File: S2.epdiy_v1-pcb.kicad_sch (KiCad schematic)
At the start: 93 parts, among them J2 Jack-DC, P1 CONN_02X13, Q1 MMBT3904, Q2 MMBT3904, SW1 RESET, SW2 BOOT, U1 MCP1700-3302E_SOT23, U3 QFN50P700X700X100-49N, U7 TPS2113APWR

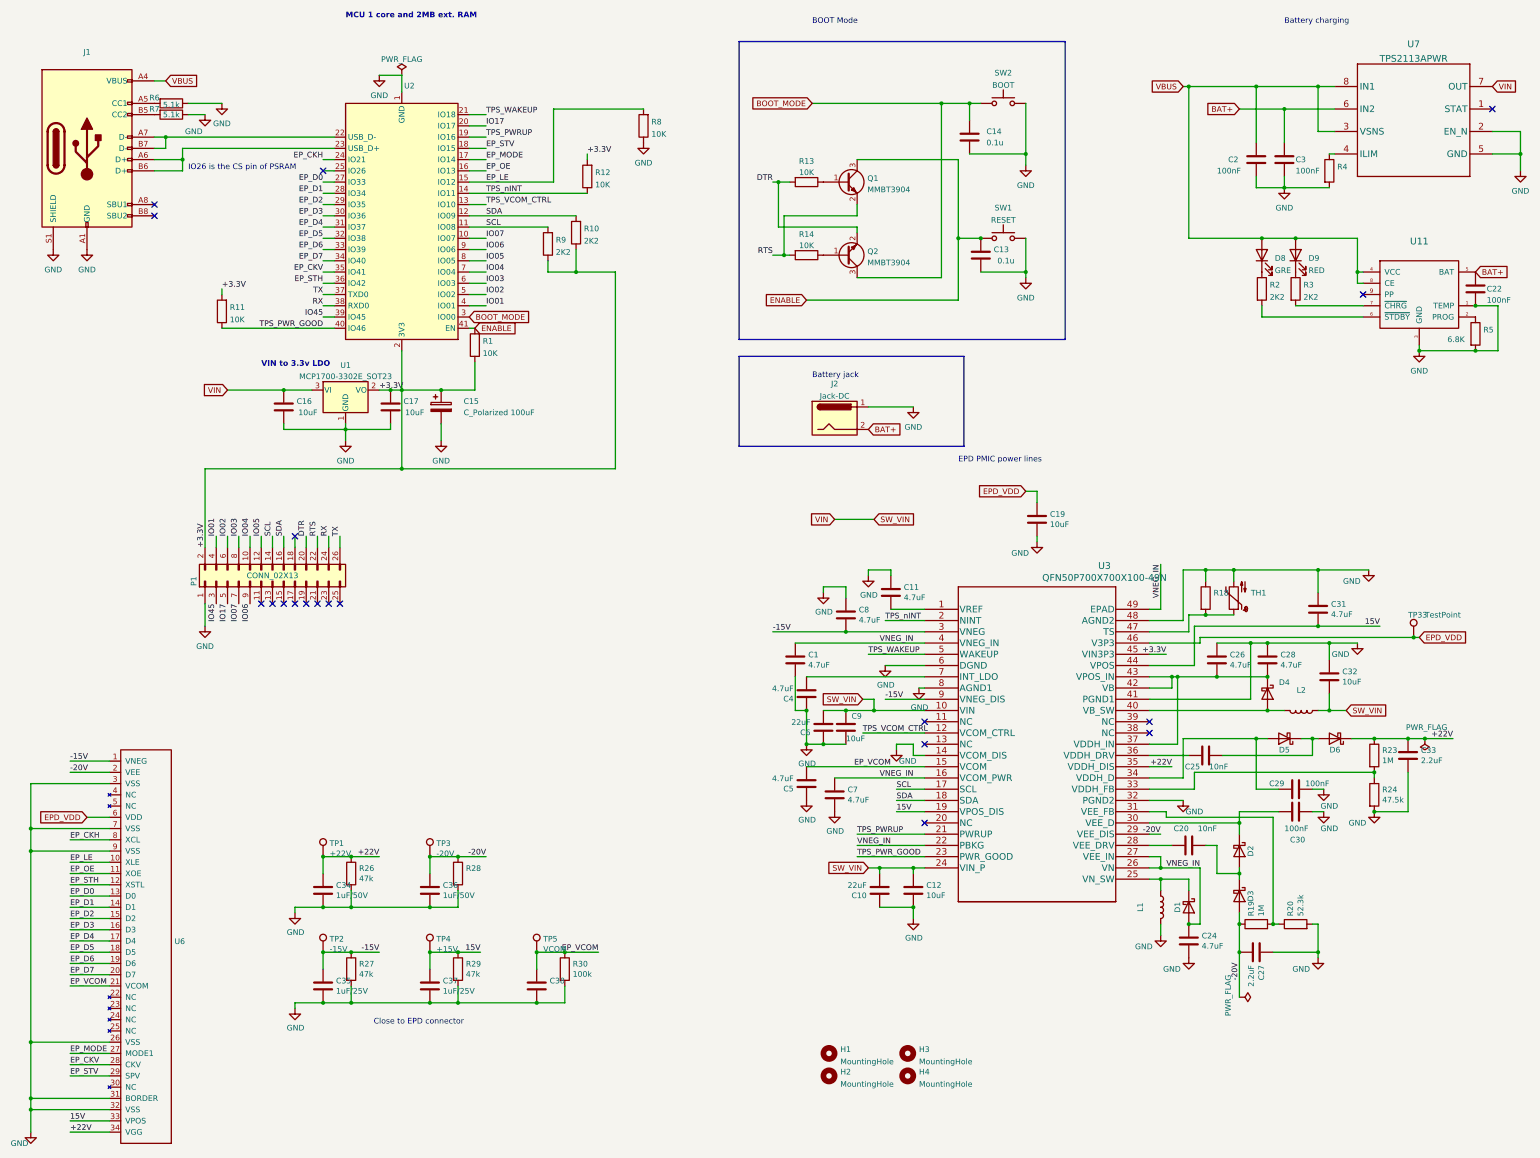
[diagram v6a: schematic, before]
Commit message: 6 10K RES wrong component 5.1Ω
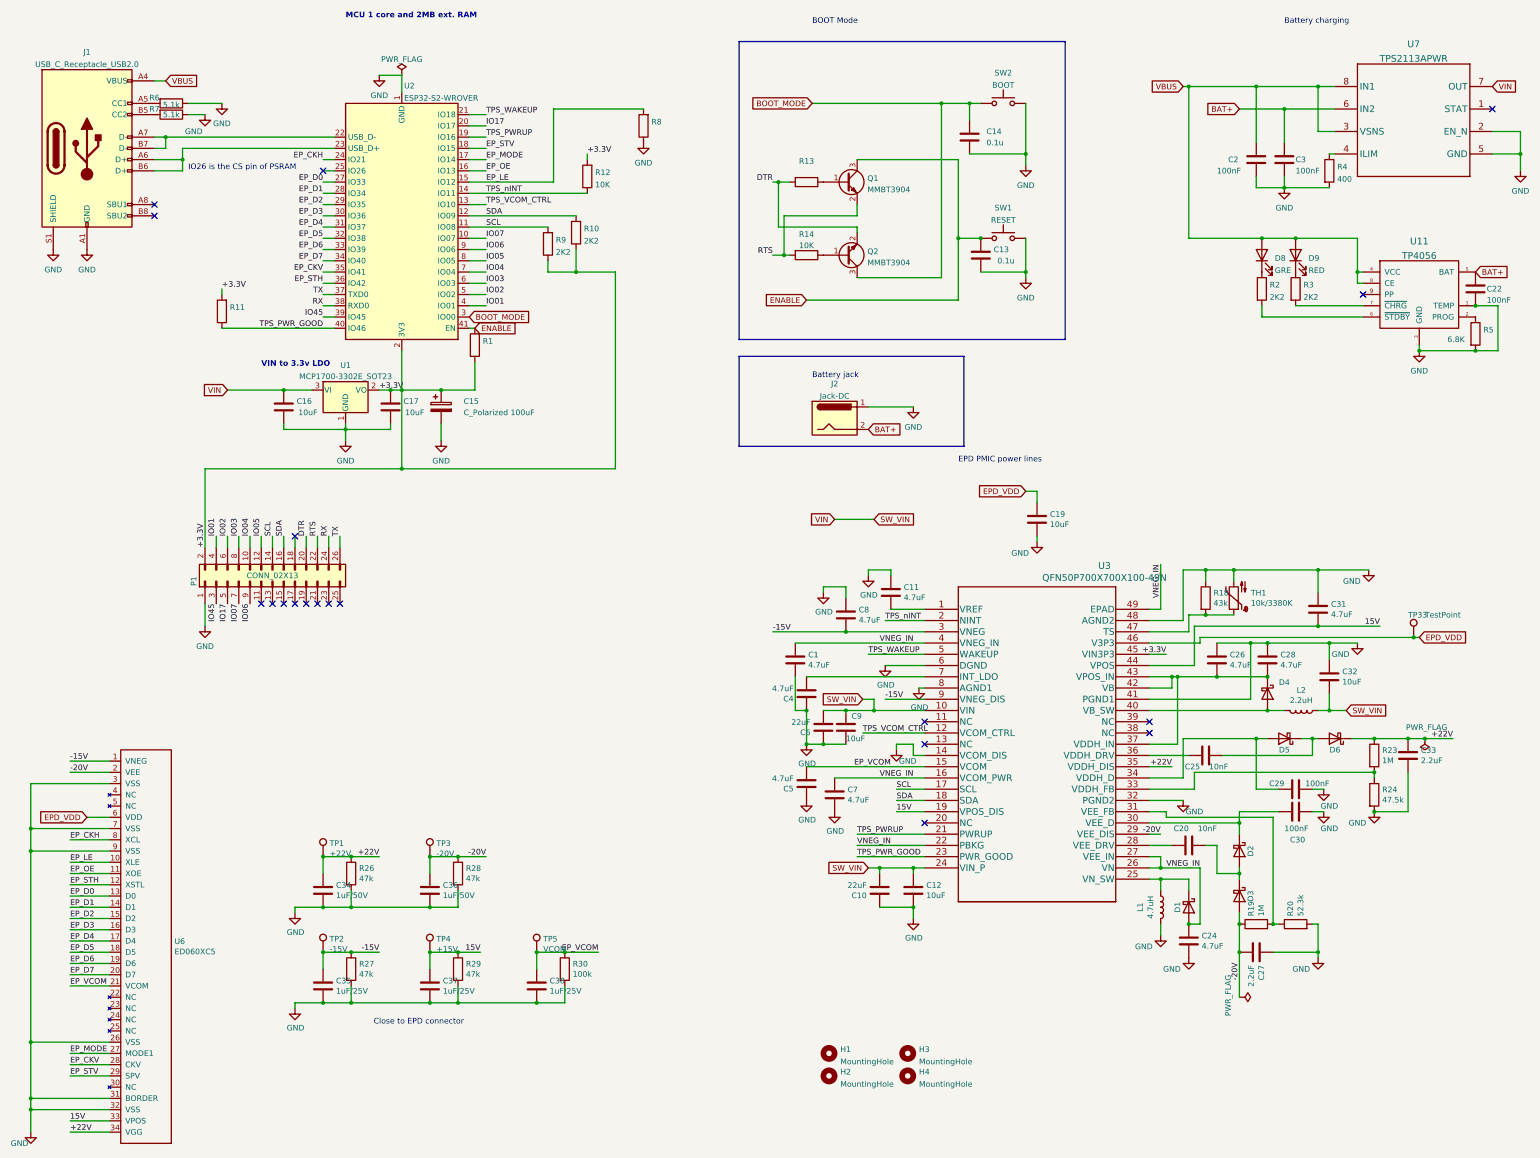
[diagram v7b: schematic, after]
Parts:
- C38: value (none) -> 1uF/25V; footprint (none) -> Capacitor_SMD:C_0805_2012Metric
- J1: value (none) -> USB_C_Receptacle_USB2.0; footprint (none) -> footprint:USB_C_Receptacle_HRO_TYPE-C-31-M-12
- L1: value (none) -> 4.7uH; footprint (none) -> Inductor_SMD:L_Taiyo-Yuden_NR-50xx_HandSoldering
- L2: value (none) -> 2.2uH; footprint (none) -> Inductor_SMD:L_Taiyo-Yuden_NR-40xx_HandSoldering
- R1, R11, R13, R8: value 10K -> (none); footprint Resistor_SMD:R_0603_1608Metric -> (none); LCSC C25197 -> C25804
- R18: value (none) -> 43k; footprint (none) -> Resistor_SMD:R_0603_1608Metric
- R28: value (none) -> 47k; footprint (none) -> Resistor_SMD:R_0603_1608Metric
- R4: value (none) -> 400; footprint (none) -> Resistor_SMD:R_0603_1608Metric
- TH1: value (none) -> 10k/3380K; footprint (none) -> Resistor_SMD:R_0603_1608Metric
- U11: value (none) -> TP4056; footprint (none) -> TP4056:TP4056_SOP-8-PP
- U2: value (none) -> ESP32-S2-WROVER; footprint (none) -> RF_Module:ESP32-S2-WROVER
- U6: value (none) -> ED060XC5; footprint (none) -> footprint:X05A20H34G
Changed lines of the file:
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@@
     (in_bom yes) (on_board yes)
     (property "Reference" "L2" (id 0) (at 335.28 173.2026 90))
-    (property "Value" "" (id 1) (at 335.28 175.514 90))
-    (property "Footprint" "" (id 2) (at 335.28 177.8 0)
+    (property "Value" "2.2uH" (id 1) (at 335.28 175.514 90))
+    (property "Footprint" "Inductor_SMD:L_Taiyo-Yuden_NR-40xx_HandSoldering" (id 2) (at 335.28 177.8 0)
       (effects (font (size 1.27 1.27)) hide)
     )
@@
       (effects (font (size 1.27 1.27)) (justify left))
     )
-    (property "Value" "" (id 1) (at 80.7212 232.283 0)
-      (effects (font (size 1.27 1.27)) (justify left))
-    )
-    (property "Footprint" "" (id 2) (at 67.31 184.15 0)
+    (property "Value" "ED060XC5" (id 1) (at 80.7212 232.283 0)
+      (effects (font (size 1.27 1.27)) (justify left))
+    )
+    (property "Footprint" "footprint:X05A20H34G" (id 2) (at 67.31 184.15 0)
       (effects (font (size 1.27 1.27)) hide)
     )
@@
       (effects (font (size 1.27 1.27)) (justify right))
     )
-    (property "Value" "" (id 1) (at 323.9008 153.543 0)
-      (effects (font (size 1.27 1.27)) (justify right))
-    )
-    (property "Footprint" "" (id 2) (at 320.04 153.67 0)
+    (property "Value" "10k/3380K" (id 1) (at 323.9008 153.543 0)
+      (effects (font (size 1.27 1.27)) (justify right))
+    )
+    (property "Footprint" "Resistor_SMD:R_0603_1608Metric" (id 2) (at 320.04 153.67 0)
       (effects (font (size 1.27 1.27)) hide)
     )
@@
       (effects (font (size 1.27 1.27)) (justify left))
     )
-    (property "Value" "" (id 1) (at 315.468 153.543 0)
-      (effects (font (size 1.27 1.27)) (justify left))
-    )
-    (property "Footprint" "" (id 2) (at 311.912 152.4 90)
+    (property "Value" "43k" (id 1) (at 315.468 153.543 0)
+      (effects (font (size 1.27 1.27)) (justify left))
+    )
+    (property "Footprint" "Resistor_SMD:R_0603_1608Metric" (id 2) (at 311.912 152.4 90)
       (effects (font (size 1.27 1.27)) hide)
     )
@@
     (in_bom yes) (on_board yes)
     (property "Reference" "L1" (id 0) (at 298.9326 222.25 90))
-    (property "Value" "" (id 1) (at 301.244 222.25 90))
-    (property "Footprint" "" (id 2) (at 303.53 222.25 0)
+    (property "Value" "4.7uH" (id 1) (at 301.244 222.25 90))
+    (property "Footprint" "Inductor_SMD:L_Taiyo-Yuden_NR-50xx_HandSoldering" (id 2) (at 303.53 222.25 0)
       (effects (font (size 1.27 1.27)) hide)
     )
@@
       (effects (font (size 1.27 1.27)) (justify left))
     )
-    (property "Value" "" (id 1) (at 146.558 215.773 0)
-      (effects (font (size 1.27 1.27)) (justify left))
-    )
-    (property "Footprint" "" (id 2) (at 143.002 214.63 90)
+    (property "Value" "47k" (id 1) (at 146.558 215.773 0)
+      (effects (font (size 1.27 1.27)) (justify left))
+    )
+    (property "Footprint" "Resistor_SMD:R_0603_1608Metric" (id 2) (at 143.002 214.63 90)
       (effects (font (size 1.27 1.27)) hide)
     )
@@
       (effects (font (size 1.27 1.27)) (justify left))
     )
-    (property "Value" "" (id 1) (at 165.481 241.173 0)
-      (effects (font (size 1.27 1.27)) (justify left))
-    )
-    (property "Footprint" "" (id 2) (at 163.5252 243.84 0)
+    (property "Value" "1uF/25V" (id 1) (at 165.481 241.173 0)
+      (effects (font (size 1.27 1.27)) (justify left))
+    )
+    (property "Footprint" "Capacitor_SMD:C_0805_2012Metric" (id 2) (at 163.5252 243.84 0)
       (effects (font (size 1.27 1.27)) hide)
     )
@@
     (in_bom yes) (on_board yes) (fields_autoplaced)
     (property "Reference" "R13" (id 0) (at 223.52 53.7042 90))
-    (property "Value" "10K" (id 1) (at 223.52 56.2411 90))
-    (property "Footprint" "Resistor_SMD:R_0603_1608Metric" (id 2) (at 223.52 56.642 90)
+    (property "Value" "" (id 1) (at 223.52 56.2411 90))
+    (property "Footprint" "" (id 2) (at 223.52 56.642 90)
       (effects (font (size 1.27 1.27)) hide)
     )
@@
       (effects (font (size 1.27 1.27)) hide)
     )
-    (property "LCSC" "C25197" (id 4) (at 223.52 58.42 90)
+    (property "LCSC" "C25804" (id 4) (at 223.52 58.42 90)
       (effects (font (size 1.27 1.27)) hide)
     )
@@
       (effects (font (size 1.27 1.27)) (justify left))
     )
-    (property "Value" "" (id 1) (at 343.408 57.7466 0)
-      (effects (font (size 1.27 1.27)) (justify left))
-    )
-    (property "Footprint" "" (id 2) (at 339.852 55.88 90)
+    (property "Value" "400" (id 1) (at 343.408 57.7466 0)
+      (effects (font (size 1.27 1.27)) (justify left))
+    )
+    (property "Footprint" "Resistor_SMD:R_0603_1608Metric" (id 2) (at 339.852 55.88 90)
       (effects (font (size 1.27 1.27)) hide)
     )
@@
       (effects (font (size 1.27 1.27)) (justify right))
     )
-    (property "Value" "" (id 1) (at 132.6006 39.4486 0)
-      (effects (font (size 1.27 1.27)) (justify right))
-    )
-    (property "Footprint" "" (id 2) (at 113.03 36.83 0)
+    (property "Value" "ESP32-S2-WROVER" (id 1) (at 132.6006 39.4486 0)
+      (effects (font (size 1.27 1.27)) (justify right))
+    )
+    (property "Footprint" "RF_Module:ESP32-S2-WROVER" (id 2) (at 113.03 36.83 0)
       (effects (font (size 1.27 1.27)) hide)
     )
@@
       (effects (font (size 1.27 1.27)) (justify right))
     )
-    (property "Value" "10K" (id 1) (at 93.218 89.4966 0)
-      (effects (font (size 1.27 1.27)) (justify right))
-    )
-    (property "Footprint" "Resistor_SMD:R_0603_1608Metric" (id 2) (at 93.218 87.63 90)
+    (property "Value" "" (id 1) (at 93.218 89.4966 0)
+      (effects (font (size 1.27 1.27)) (justify right))
+    )
+    (property "Footprint" "" (id 2) (at 93.218 87.63 90)
       (effects (font (size 1.27 1.27)) hide)
     )
@@
       (effects (font (size 1.27 1.27)) hide)
     )
-    (property "LCSC" "C25197" (id 4) (at 91.44 87.63 0)
+    (property "LCSC" "C25804" (id 4) (at 91.44 87.63 0)
       (effects (font (size 1.27 1.27)) hide)
     )
@@
       (effects (font (size 1.27 1.27)) (justify right))
     )
-    (property "Value" "10K" (id 1) (at 188.468 47.5866 0)
-      (effects (font (size 1.27 1.27)) (justify right))
-    )
-    (property "Footprint" "Resistor_SMD:R_0603_1608Metric" (id 2) (at 188.468 45.72 90)
+    (property "Value" "" (id 1) (at 188.468 47.5866 0)
+      (effects (font (size 1.27 1.27)) (justify right))
+    )
+    (property "Footprint" "" (id 2) (at 188.468 45.72 90)
       (effects (font (size 1.27 1.27)) hide)
     )
@@
       (effects (font (size 1.27 1.27)) hide)
     )
-    (property "LCSC" "C25197" (id 4) (at 186.69 45.72 0)
+    (property "LCSC" "C25804" (id 4) (at 186.69 45.72 0)
       (effects (font (size 1.27 1.27)) hide)
     )
@@
     (in_bom yes) (on_board yes) (fields_autoplaced)
     (property "Reference" "J1" (id 0) (at 60.96 29.0535 0))
-    (property "Value" "" (id 1) (at 60.96 31.8286 0))
-    (property "Footprint" "" (id 2) (at 64.77 50.8 0)
+    (property "Value" "USB_C_Receptacle_USB2.0" (id 1) (at 60.96 31.8286 0))
+    (property "Footprint" "footprint:USB_C_Receptacle_HRO_TYPE-C-31-M-12" (id 2) (at 64.77 50.8 0)
       (effects (font (size 1.27 1.27)) hide)
     )
@@
       (effects (font (size 1.524 1.524)))
     )
-    (property "Value" "" (id 1) (at 361.95 75.0751 0)
+    (property "Value" "TP4056" (id 1) (at 361.95 75.0751 0)
       (effects (font (size 1.524 1.524)))
     )
-    (property "Footprint" "" (id 2) (at 361.95 75.0751 0)
+    (property "Footprint" "TP4056:TP4056_SOP-8-PP" (id 2) (at 361.95 75.0751 0)
       (effects (font (size 1.524 1.524)) hide)
     )
@@
       (effects (font (size 1.27 1.27)) (justify right))
     )
-    (property "Value" "10K" (id 1) (at 150.368 97.1166 0)
-      (effects (font (size 1.27 1.27)) (justify right))
-    )
-    (property "Footprint" "Resistor_SMD:R_0603_1608Metric" (id 2) (at 150.368 95.25 90)
+    (property "Value" "" (id 1) (at 150.368 97.1166 0)
+      (effects (font (size 1.27 1.27)) (justify right))
+    )
+    (property "Footprint" "" (id 2) (at 150.368 95.25 90)
       (effects (font (size 1.27 1.27)) hide)
     )
@@
       (effects (font (size 1.27 1.27)) hide)
     )
-    (property "LCSC" "C25197" (id 4) (at 148.59 95.25 0)
-      (effects (font (size 1.27 1.27)) hide)
-    )
+    (property "LCSC" "C25804" (id 4) (at 148.59 95.25 0)
+      (effects (font (size 1.27 1.27)) hide)
+    )
